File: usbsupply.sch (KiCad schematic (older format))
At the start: 62 parts, among them P1 USB_OTG, P2 SWD_CONN, P3 VOUT_CONN, P4 GND_CONN, Q1 BSS138, Q2 FDG332PZ, Q3 FDS6982AS, U1 IP4234CZ6, U2 MIC5504-3.3, U3 LTC3883EUH-1#PBF

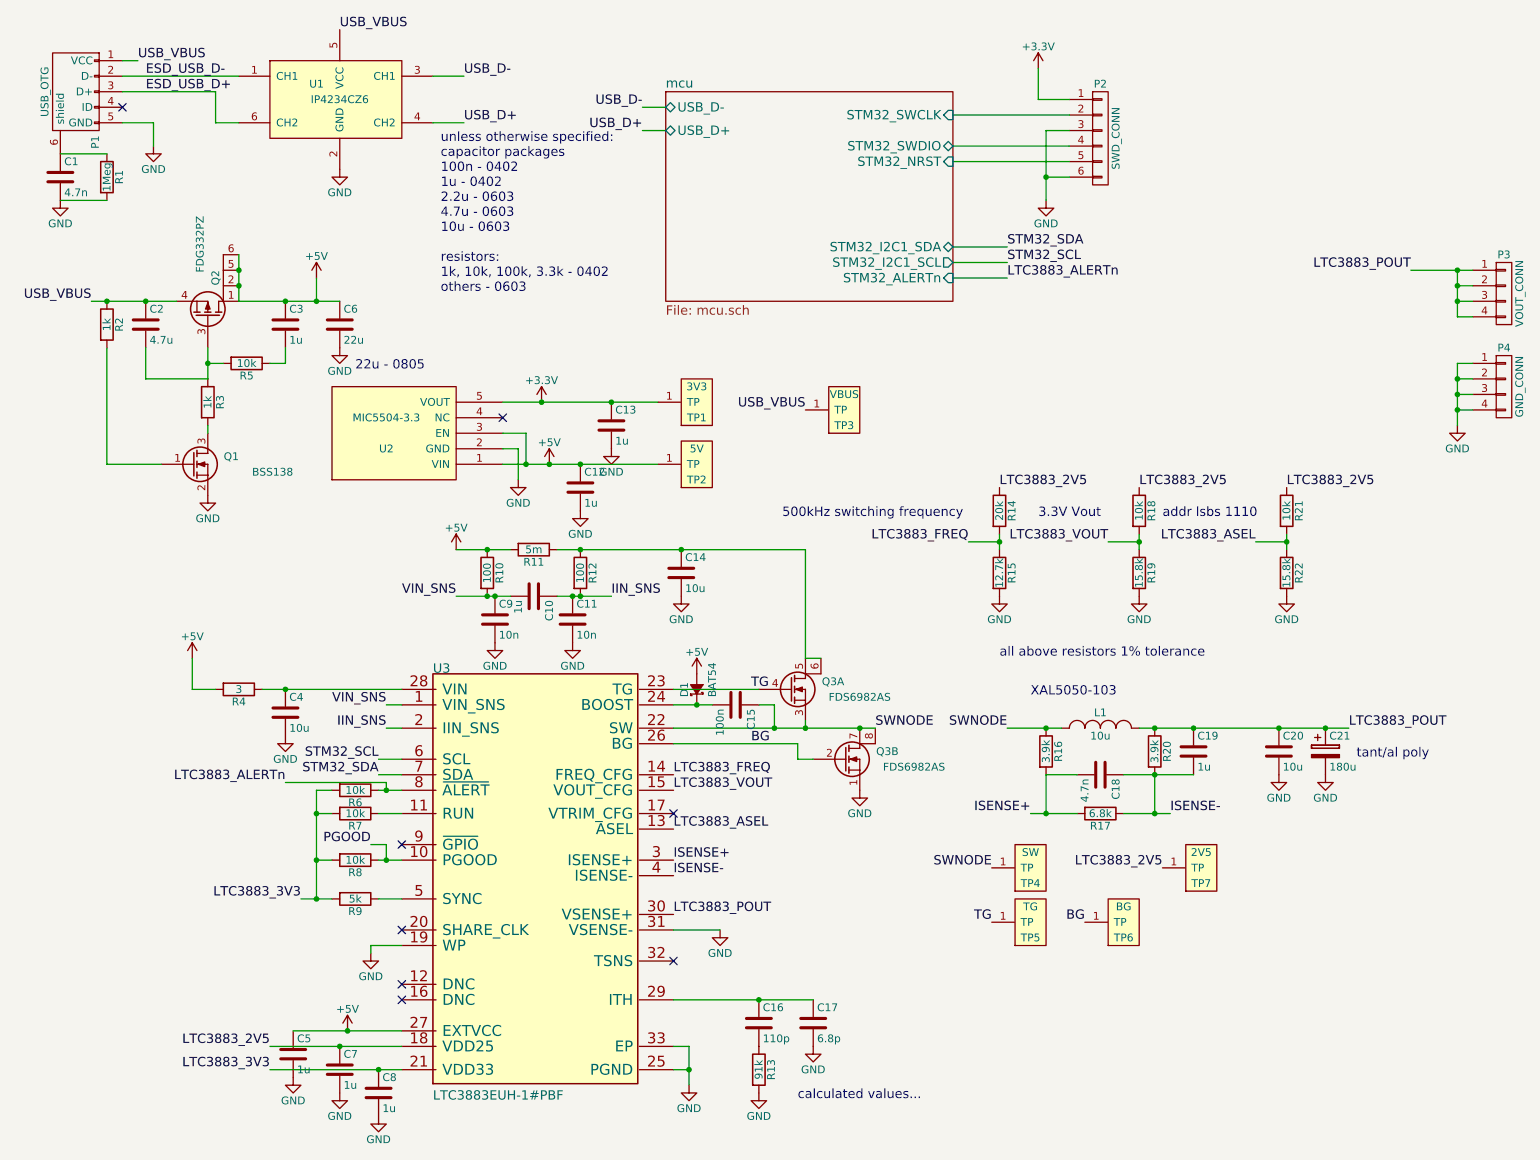
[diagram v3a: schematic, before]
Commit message: Finish layout and routing of initial PCB revision.
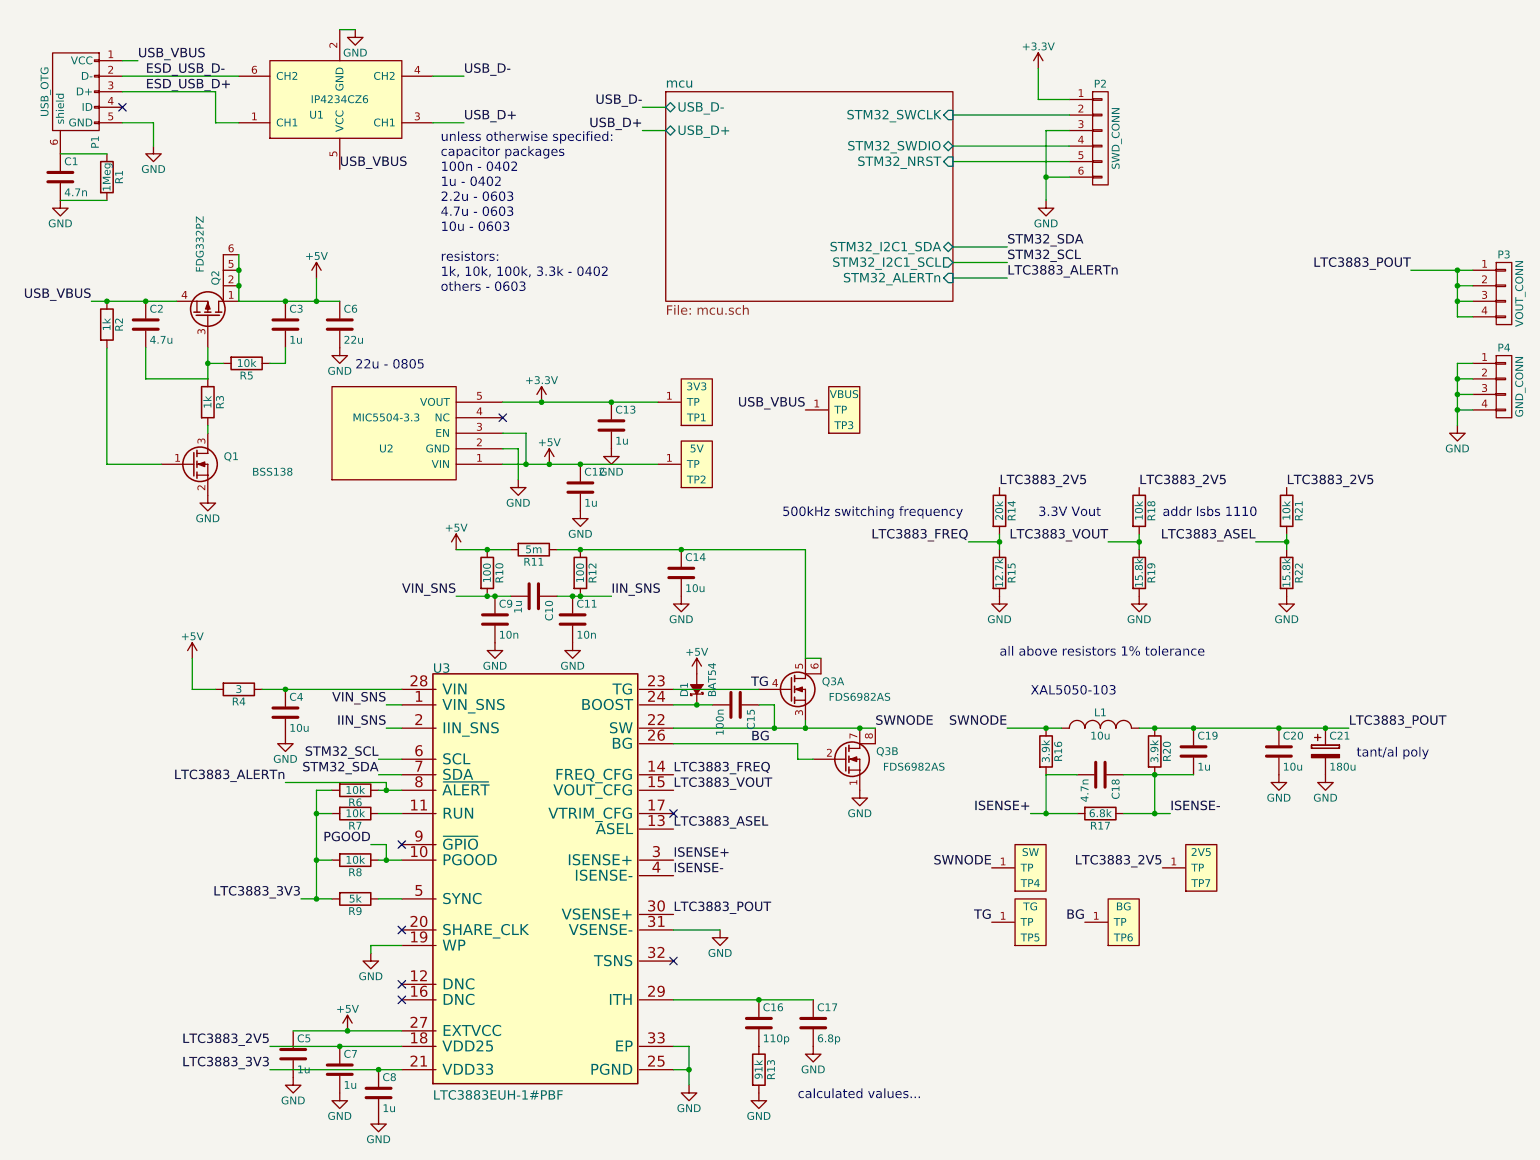
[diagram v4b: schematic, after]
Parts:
- C1, C14, C16, C17, C18, C2, C20, C4: footprint (none) -> Capacitors_SMD:C_0603
- C10, C11, C12, C13, C15, C19, C3, C5, C7, C8, C9: footprint (none) -> Capacitors_SMD:C_0402
- C21: footprint (none) -> Capacitors_Tantalum_SMD:TantalC_SizeD_EIA-7343_Reflow
- C6: footprint (none) -> Capacitors_SMD:C_0805
- D1, Q1: footprint (none) -> TO_SOT_Packages_SMD:SOT-23
- L1: footprint (none) -> kicad-fp:XAL5050
- P1: footprint (none) -> Connect:USB_Mini-B
- P2: footprint (none) -> Pin_Headers:Pin_Header_Straight_1x06
- P3, P4: footprint (none) -> Pin_Headers:Pin_Header_Straight_1x04
- Q2: footprint (none) -> TO_SOT_Packages_SMD:SC-70-6
- Q3: footprint (none) -> Housings_SOIC:SOIC-8_3.9x4.9mm_Pitch1.27mm
- R1, R4: footprint (none) -> Resistors_SMD:R_0805
- R10, R12, R18, R2, R21, R3, R5, R6, R7, R8: footprint (none) -> Resistors_SMD:R_0402
- R11: footprint (none) -> Resistors_SMD:R_1206
- R13, R14, R15, R16, R17, R19, R20, R22, R9: footprint (none) -> Resistors_SMD:R_0603
- TP1, TP2, TP3, TP4, TP5, TP6, TP7: footprint MODULE -> bce:TP
- U1: footprint (none) -> sot:SOT457
- U2: footprint MODULE -> TO_SOT_Packages_SMD:SOT-23-5
- U3: footprint (none) -> Housings_DFN_QFN:QFN-32-1EP_5x5mm_Pitch0.5mm
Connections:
- net ESD_USB_D+: now also U1.1 (CH1); no longer U1.6 (CH2)
- net ESD_USB_D-: now also U1.6 (CH2); no longer U1.1 (CH1)
- net USB_D+: now also U1.3 (CH1); no longer U1.4 (CH2)
- net USB_D-: now also U1.4 (CH2); no longer U1.3 (CH1)
